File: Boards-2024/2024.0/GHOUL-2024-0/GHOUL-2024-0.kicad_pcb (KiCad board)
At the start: 4 copper layers, 91 parts, among them J1 USB_C_Receptacle_USB2.0, J2 U.FL, J3 SOICbite, J4 Conn_01x03_Pin, Q1 Q_NMOS_GSD, SW2 SLIDE, U1 MCU_RaspberryPi_RP2040_RP2040, U11 MAX-M10S, U2 TVS1800DRVR, U3 USBLC6-2SC6, U4 TPS2121RUXR, U5 W25Q128JVS, U6 LT6703CDC-3, U7 DRF1262TL, U8 MB85RS1MT, U9 MS5607-02BA, Y1 12MHz

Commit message: starting board layout
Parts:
- added TP1: TestPoint, TestPoint:TestPoint_Keystone_5000-5004_Miniature, F.Cu at (92.4, 73.8)
- added TP2: TestPoint, TestPoint:TestPoint_Keystone_5000-5004_Miniature, F.Cu at (92.5, 84.7)
- added U10: LTM4622AEV-PBF, GHOUL2024:LGA25_6P25X6P25_ADI, F.Cu at (89.5, 79.2)
- moved C23 132.4 mm to (160.1, 114.3), turned to -90 degrees
- moved C37 122.0 mm to (163.1, 144.0)
- moved AE1 122.0 mm to (178.7, 149.7)
- moved C35 122.0 mm to (163.0, 145.7)
- moved D2 122.0 mm to (159.4, 147.3)
- moved J4 122.0 mm to (160.2, 135.4)
- moved R24 122.0 mm to (178.3, 140.4)
- moved R28 122.0 mm to (159.7, 144.0)
- moved U11 122.0 mm to (170.7, 142.6)
- moved BT2 122.0 mm to (161.4, 140.0)
- moved R25 122.0 mm to (178.2, 138.8)
- moved U8 104.2 mm to (157.7, 117.8), turned to 90 degrees
- moved C16 79.8 mm to (113.8, 63.2)
- moved C17 78.1 mm to (112.0, 66.4)
- moved U2 77.8 mm to (113.6, 60.8)
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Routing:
- net +3V3: track 0.00 -> 23.2 mm, vias 0 -> 1
- net /QSPI_SS: track 0.00 -> 14.0 mm
- net GND: track 0.00 -> 13.0 mm, vias 0 -> 3
- net /QSPI_SD1: track 0.00 -> 12.8 mm
- net /QSPI_SD2: track 0.00 -> 11.4 mm
- net +1V1: track 0.00 -> 10.9 mm
- net Net-(U1-RUN): track 0.00 -> 9.54 mm
- net Net-(U1-XIN): track 0.00 -> 7.02 mm
- net Net-(U1-USB_DP): track 0.00 -> 6.58 mm
- net /QSPI_SD3: track 0.00 -> 6.24 mm
- net /RP_SWD: track 0.00 -> 6.07 mm
- net /RP_SWCLK: track 0.00 -> 5.69 mm
- net /FRAM_CS: track 0.00 -> 5.48 mm
- net /QSPI_SCLK: track 0.00 -> 4.91 mm
- net Net-(U1-USB_DM): track 0.00 -> 4.74 mm
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- added copper zone on In1.Cu, net GND
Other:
- board outline added: 60 x 60 mm

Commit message: finished connecting everything
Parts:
- added D3: LED, LED_SMD:LED_0603_1608Metric, F.Cu at (150.4, 138.3)
- added D4: LED, LED_SMD:LED_0603_1608Metric, F.Cu at (150.4, 145.2)
- added D5: LED, LED_SMD:LED_0603_1608Metric, F.Cu at (150.4, 141.8)
- added D6: LED, LED_SMD:LED_0603_1608Metric, F.Cu at (150.4, 134.8)
- added Q2: Q_NMOS_GSD, Package_TO_SOT_SMD:SOT-23-3, F.Cu at (146.7, 137.8)
- added Q3: Q_NMOS_GSD, Package_TO_SOT_SMD:SOT-23-3, F.Cu at (146.7, 144.7)
- added Q4: Q_NMOS_GSD, Package_TO_SOT_SMD:SOT-23-3, F.Cu at (146.7, 141.3)
- added Q5: Q_NMOS_GSD, Package_TO_SOT_SMD:SOT-23-3, F.Cu at (146.7, 134.3)
- added R27: 470, Resistor_SMD:R_0603_1608Metric, F.Cu at (150.4, 136.7)
- added R29: 470, Resistor_SMD:R_0603_1608Metric, F.Cu at (150.4, 143.7)
- added R30: 470, Resistor_SMD:R_0603_1608Metric, F.Cu at (150.4, 140.2)
- added R31: 470, Resistor_SMD:R_0603_1608Metric, F.Cu at (150.4, 133.2)
- C21, C22, J2, U7: moved to B.Cu
- moved H2 162.3 mm to (185.9, 154.0)
- moved H4 127.0 mm to (185.2, 84.3)
- moved R21 118.9 mm to (157.8, 107.1), turned to 90 degrees
- moved C27 118.8 mm to (165.3, 105.2), turned to 90 degrees
- moved H3 118.6 mm to (121.4, 159.0)
- moved R20 115.0 mm to (152.0, 108.7)
- moved C24 109.6 mm to (154.2, 106.7)
- moved L2 107.1 mm to (161.5, 106.4), turned to 180 degrees
- moved C21 101.0 mm to (156.5, 133.5)
- moved J2 101.0 mm to (160.7, 133.6)
- moved C22 97.7 mm to (156.6, 131.8)
- moved L1 97.1 mm to (149.8, 105.1), turned to 90 degrees
- moved J1 94.7 mm to (176.3, 109.7), turned to 90 degrees
- moved R3 89.7 mm to (170.6, 113.3), turned to 90 degrees
- moved BT1 82.3 mm to (166.8, 97.1), turned to -90 degrees
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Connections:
- C25 pad 1: +3.3V -> Net-(C25-Pad1)
- C26 pad 1: +5V -> Net-(C26-Pad1)
- L1 pad 2: Net-(L1-Pad2) -> Net-(C26-Pad1)
- L2 pad 2: Net-(L2-Pad2) -> Net-(C25-Pad1)
- Q1 pad 1: /LED -> /LED5
- R20 pad 2: Net-(L1-Pad2) -> Net-(C26-Pad1)
- R21 pad 2: Net-(L2-Pad2) -> Net-(C25-Pad1)
- U1 pad 2: /LED -> /LED1
- U1 pad 3: unconnected-(U1-GPIO1-Pad3) -> /LED2
- U1 pad 4: unconnected-(U1-GPIO2-Pad4) -> /LED3
- U1 pad 5: unconnected-(U1-GPIO3-Pad5) -> /LED4
- U1 pad 6: unconnected-(U1-GPIO4-Pad6) -> /LED5
- U10 pad A1: +5V -> Net-(C26-Pad1)
- U10 pad B1: +5V -> Net-(C26-Pad1)
- U10 pad D1: +3.3V -> Net-(C25-Pad1)
- U10 pad E1: +3.3V -> Net-(C25-Pad1)
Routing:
- net GND: track 13.0 -> 116.5 mm, vias 3 -> 109
- net +3V3: track 23.2 -> 86.8 mm, vias 1 -> 13
- net VBUS: track 0.00 -> 49.0 mm, vias 0 -> 6
- net +5V: track 0.00 -> 43.7 mm, vias 0 -> 4
- net VCC: track 0.00 -> 36.7 mm
- net /LED1: track 0.00 -> 33.6 mm
- net /SCL: track 0.00 -> 33.4 mm, vias 0 -> 2
- net /SDA: track 0.00 -> 31.0 mm
- net /LED2: track 0.00 -> 29.6 mm
- net /DRF_DIO1: track 0.00 -> 29.4 mm, vias 0 -> 1
- net /DRF_BUSY: track 0.00 -> 27.5 mm, vias 0 -> 1
- net /LED3: track 0.00 -> 24.9 mm
- net /RDIO_RST: track 1.20 -> 23.8 mm
- net /LVC_CUTOFF: track 0.00 -> 20.7 mm, vias 0 -> 2
- net /LED4: track 0.00 -> 20.6 mm
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- added copper zone on In2.Cu, net +3V3
- added copper zone on In2.Cu, net +5V
- added copper zone on F.Cu, net +BATT
- added copper zone on B.Cu, net GND
- added copper zone on F.Cu, net GND
- added copper zone on F.Cu, net VBUS
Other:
- board size 60 x 60 mm -> 57 x 60 mm

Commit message: finished board
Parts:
- added J10: Conn_01x04, Connector_PinHeader_2.54mm:PinHeader_1x04_P2.54mm_Vertical, F.Cu at (156.9, 147.1)
- added J5: Conn_01x04, Connector_Molex:Molex_SL_171971-0004_1x04_P2.54mm_Vertical, B.Cu at (138.1, 98.9)
- added J6: Conn_01x03, Connector_Molex:Molex_SL_171971-0003_1x03_P2.54mm_Vertical, F.Cu at (138.1, 106.9)
- added J7: Conn_01x02, Connector_Molex:Molex_SL_171971-0002_1x02_P2.54mm_Vertical, F.Cu at (138.1, 132.2)
- added J8: Conn_01x02, Connector_Molex:Molex_SL_171971-0002_1x02_P2.54mm_Vertical, F.Cu at (138.1, 141.1)
- added J9: Conn_01x04, Connector_Molex:Molex_SL_171971-0004_1x04_P2.54mm_Vertical, F.Cu at (138.1, 118.4)
- added Q6: Q_NMOS_GSD, Package_TO_SOT_SMD:SC-59, F.Cu at (160.6, 112.9)
- added Q7: Q_NMOS_GSD, Package_TO_SOT_SMD:SC-59, F.Cu at (164.7, 112.9)
- added R32: 4.7k, Resistor_SMD:R_0603_1608Metric, F.Cu at (142.3, 115.7)
- moved SW2 1.18 mm to (144.2, 93.2)
- moved C7 0.81 mm to (145.3, 120.1), turned to -135 degrees
- moved C3 0.69 mm to (150.6, 126.6), turned to 0 degrees
- moved C8 0.43 mm to (146.2, 115.1)
- moved R1 0.26 mm to (150.7, 123.6)
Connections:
- U1 pad 15: unconnected-(U1-GPIO12-Pad15) -> /LED4
- U1 pad 17: unconnected-(U1-GPIO14-Pad17) -> /HEATER1
- U1 pad 18: unconnected-(U1-GPIO15-Pad18) -> /HEATER2
- U1 pad 27: unconnected-(U1-GPIO16-Pad27) -> /GPIO16
- U1 pad 30: unconnected-(U1-GPIO19-Pad30) -> /GPIO19
- U1 pad 34: unconnected-(U1-GPIO22-Pad34) -> /PGOOD_CUT
- U1 pad 35: unconnected-(U1-GPIO23-Pad35) -> /DATA_CUT
- U1 pad 4: /LED3 -> /GPIO2
- U1 pad 40: unconnected-(U1-GPIO28_ADC2-Pad40) -> /CUT_CURR
- U1 pad 5: /LED4 -> /GPIO3
- U1 pad 7: unconnected-(U1-GPIO5-Pad7) -> /SERVO_PWM
- U1 pad 8: unconnected-(U1-GPIO6-Pad8) -> /TEMP
- U1 pad 9: unconnected-(U1-GPIO7-Pad9) -> /LED3
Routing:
- net /GPIO3: track 0.00 -> 51.9 mm, vias 0 -> 2
- net /GPIO2: track 0.00 -> 50.8 mm, vias 0 -> 2
- net Net-(J8-Pin_2): track 0.00 -> 50.5 mm, vias 0 -> 1
- net Net-(J7-Pin_2): track 0.00 -> 45.1 mm, vias 0 -> 1
- net +5V: track 43.7 -> 87.0 mm
- net /SERVO_PWM: track 0.00 -> 40.8 mm, vias 0 -> 1
- net /GPIO19: track 0.00 -> 33.9 mm, vias 0 -> 2
- net GND: track 116.5 -> 149.2 mm, vias 109 -> 119
- net /GPIO16: track 0.00 -> 28.8 mm, vias 0 -> 1
- net /TEMP: track 0.00 -> 28.0 mm, vias 0 -> 2
- net /HEATER2: track 0.00 -> 26.3 mm, vias 0 -> 2
- net /DATA_CUT: track 0.00 -> 23.7 mm, vias 0 -> 2
- net /CUT_CURR: track 0.00 -> 22.6 mm, vias 0 -> 1
- net /PGOOD_CUT: track 0.00 -> 21.7 mm, vias 0 -> 1
- net +3V3: track 86.8 -> 106.5 mm, vias 13 -> 20
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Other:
- board outline removed

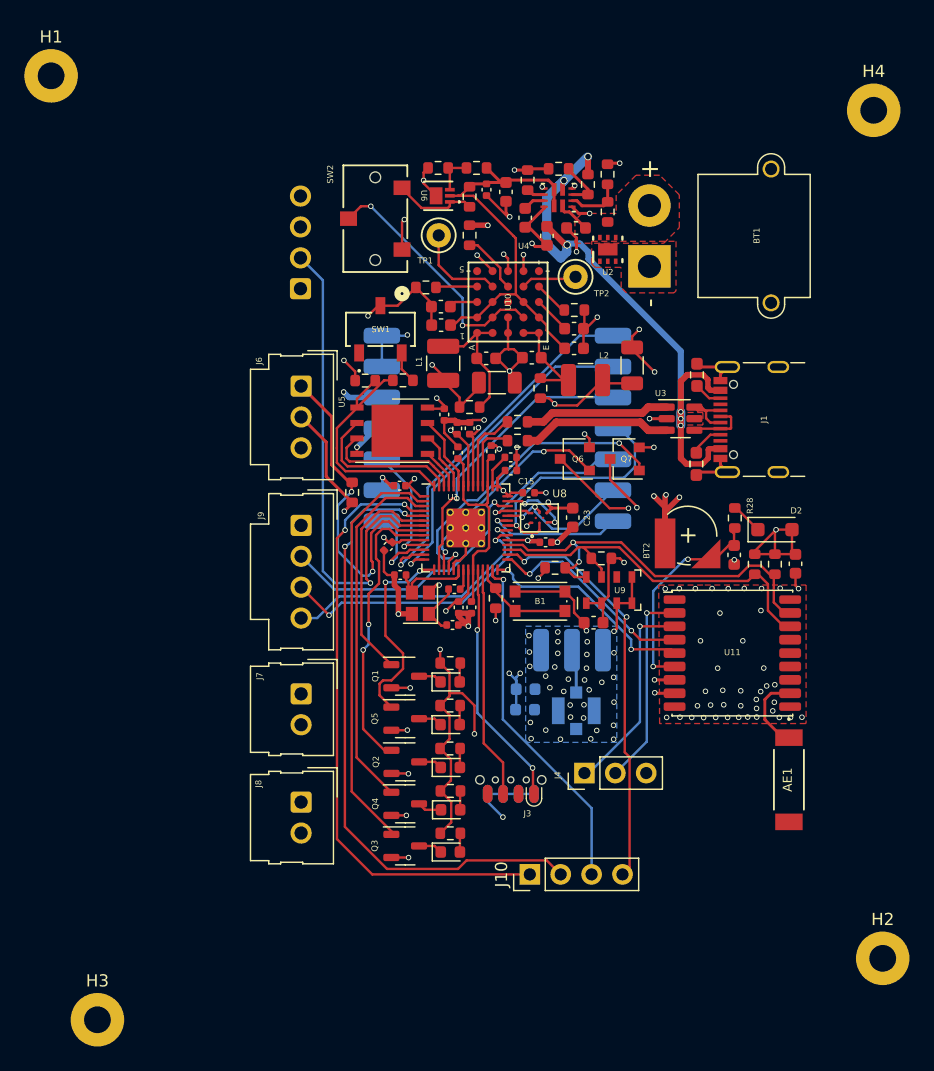
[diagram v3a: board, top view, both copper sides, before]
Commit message: Finished board outline
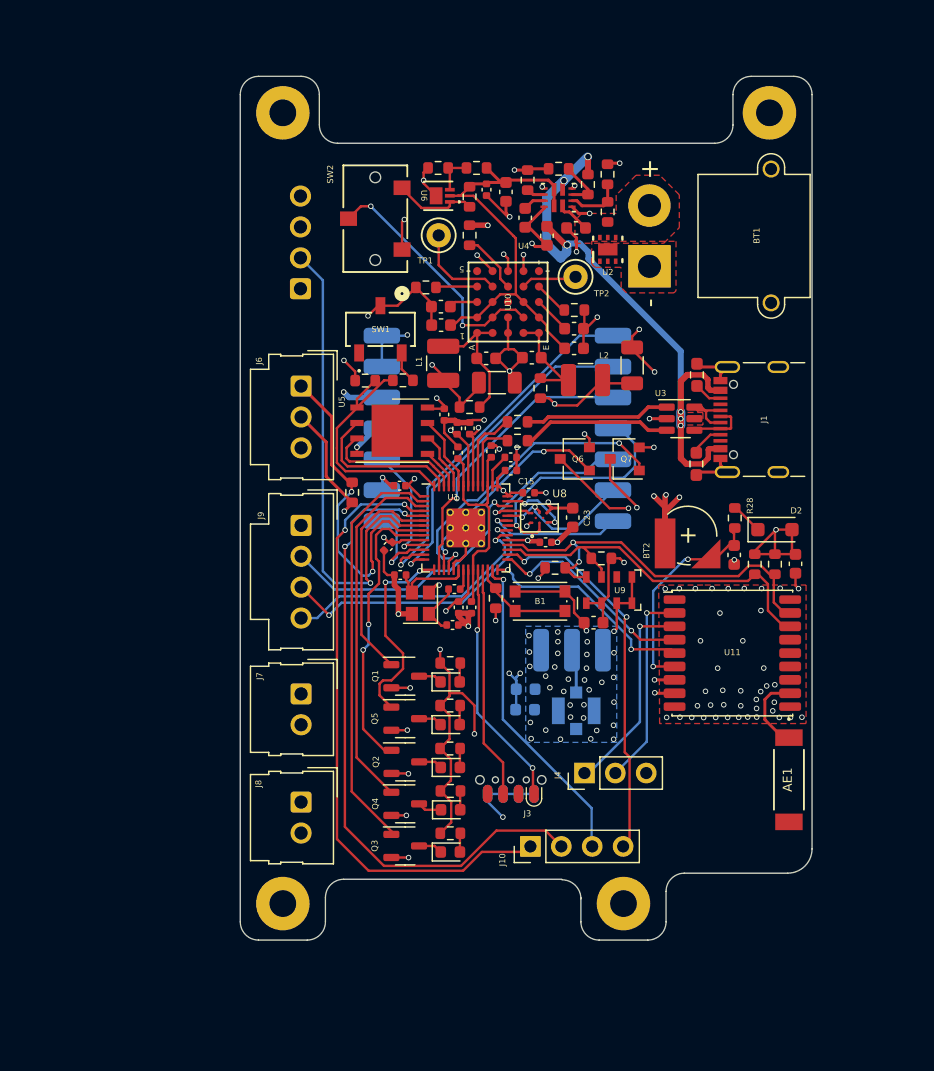
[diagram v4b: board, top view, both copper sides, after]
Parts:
- moved H2 49.5 mm to (136.6, 149.5)
- moved H3 44.3 mm to (164.6, 149.5)
- moved H1 19.3 mm to (136.6, 84.5)
- moved H4 8.57 mm to (176.6, 84.5)
- moved J10 2.30 mm to (157.0, 144.8)
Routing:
- net /GPIO19: track 33.9 -> 31.5 mm
- net /GPIO16: track 28.8 -> 26.5 mm
- net /GPIO3: track 51.9 -> 53.2 mm
- net /GPIO2: track 50.8 -> 51.5 mm
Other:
- board outline added: 47 x 71 mm

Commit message: ready for shipman review
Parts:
- C25, C26: footprint Capacitor_SMD:C_0603_1608Metric -> Capacitor_SMD:C_0805_2012Metric
- moved C21 31.8 mm to (140.7, 106.0), turned to 180 degrees
- moved C22 31.7 mm to (140.7, 104.4), turned to 180 degrees
- moved R21 0.37 mm to (157.8, 107.5)
- moved C24 0.23 mm to (154.1, 106.8)
- moved C25 0.17 mm to (157.3, 104.6)
- moved J6 0.15 mm to (138.0, 106.8)
- moved R20 0.13 mm to (152.0, 108.8)
- moved C26 0.11 mm to (153.3, 104.5)
- moved C14 0.11 mm to (152.0, 110.5)
- moved C11 0.11 mm to (151.0, 110.5)
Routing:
- net GND: track 149.2 -> 161.1 mm, vias 119 -> 126
- net +5V: track 87.0 -> 82.6 mm, vias 4 -> 5
- net +3V3: track 106.5 -> 105.5 mm, vias 20 -> 21
- net /LVC_CUTOFF: track 21.0 -> 21.7 mm
- added copper zone on F.Cu, net +3V3
- added copper zone on F.Cu, net +5V
- added copper zone on In2.Cu, net GND
- added copper zone on F.Cu, net Net-(C25-Pad1)
- added copper zone on F.Cu, net VCC
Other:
- outline, holes or cut-outs redrawn

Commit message: almost as good as garlic honey chicken
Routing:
- net VBUS: track 52.8 -> 49.3 mm
- net GND: track 161.1 -> 162.0 mm
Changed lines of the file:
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@@
   (segment (start 155.675 89.175) (end 155.67 89.17) (width 0.25) (layer "F.Cu") (net 2))
   (segment (start 146.428101 95.71) (end 146.428101 93.431899) (width 1) (layer "F.Cu") (net 2))
+  (segment (start 160.7 94.679998) (end 159.955001 93.934999) (width 0.25) (layer "F.Cu") (net 2))
   (segment (start 150.67 122.0275) (end 150.67 121.495025) (width 0.2) (layer "F.Cu") (net 2))
   (segment (start 164.075 126.825) (end 164.075 124.775) (width 0.2) (layer "F.Cu") (net 2))
@@
   (segment (start 151.06 126.57) (end 151.78 126.57) (width 0.2) (layer "F.Cu") (net 2))
   (segment (start 165.34 103.755) (end 165.34 103.92) (width 0.2) (layer "F.Cu") (net 2))
-  (segment (start 160.77 94.749998) (end 160.77 95.89) (width 0.25) (layer "F.Cu") (net 2))
   (segment (start 156.855 89.07) (end 156.75 89.175) (width 0.25) (layer "F.Cu") (net 2))
   (segment (start 161.345 102.21) (end 161.54 102.21) (width 0.2) (layer "F.Cu") (net 2))
@@
   (segment (start 158.34 95.355) (end 158.235 95.46) (width 0.25) (layer "F.Cu") (net 2))
   (segment (start 178.77 123.33) (end 179.02 123.58) (width 0.2) (layer "F.Cu") (net 2))
-  (segment (start 159.955001 93.934999) (end 160.77 94.749998) (width 0.25) (layer "F.Cu") (net 2))
+  (segment (start 160.22995 96.09) (end 160.7 95.61995) (width 0.25) (layer "F.Cu") (net 2))
   (segment (start 172.6 113.425) (end 173.175 114) (width 0.25) (layer "F.Cu") (net 2))
   (segment (start 154.12 104.655) (end 154.225 104.655) (width 0.2) (layer "F.Cu") (net 2))
@@
   (segment (start 158.71 119.77) (end 159.205 119.77) (width 0.45) (layer "F.Cu") (net 2))
   (segment (start 165.325 122.625) (end 165.325 124.775) (width 0.2) (layer "F.Cu") (net 2))
+  (segment (start 160.7 95.61995) (end 160.7 94.679998) (width 0.25) (layer "F.Cu") (net 2))
   (segment (start 148.845 101.9) (end 148.865 101.92) (width 0.2) (layer "F.Cu") (net 2))
   (segment (start 155.265 105.695) (end 155.265 106.55) (width 0.2) (layer "F.Cu") (net 2))
   (segment (start 154.225 104.655) (end 155.265 105.695) (width 0.2) (layer "F.Cu") (net 2))
   (segment (start 158.235 95.46) (end 157.78 95.46) (width 0.25) (layer "F.Cu") (net 2))
+  (segment (start 159.63 96.09) (end 160.22995 96.09) (width 0.25) (layer "F.Cu") (net 2))
   (segment (start 144.951178 120.448822) (end 144.9395 120.4605) (width 0.2) (layer "F.Cu") (net 2))
   (segment (start 150.875025 121.29) (end 151.16 121.29) (width 0.2) (layer "F.Cu") (net 2))
@@
   (via (at 176.4 131.58) (size 0.45) (drill 0.3) (layers "F.Cu" "B.Cu") (free) (net 2))
   (via (at 158.98 130.02) (size 0.45) (drill 0.3) (layers "F.Cu" "B.Cu") (free) (net 2))
-  (via (at 160.77 95.89) (size 0.45) (drill 0.3) (layers "F.Cu" "B.Cu") (net 2))
+  (via (at 159.63 96.09) (size 0.45) (drill 0.3) (layers "F.Cu" "B.Cu") (net 2))
   (via (at 146.428101 93.431899) (size 0.75) (drill 0.6) (layers "F.Cu" "B.Cu") (net 2))
   (via (at 165.93 102.27) (size 0.45) (drill 0.3) (layers "F.Cu" "B.Cu") (net 2))
@@
   (via (at 160 95.33) (size 0.75) (drill 0.6) (layers "F.Cu" "B.Cu") (net 10))
   (segment (start 161.752703 96.622703) (end 161.752703 95.592703) (width 0.75) (layer "B.Cu") (net 10))
-  (segment (start 161.25 95.09) (end 160.24 95.09) (width 0.75) (layer "B.Cu") (net 10))
+  (segment (start 159.3 90.36) (end 161.56 88.1) (width 1) (layer "B.Cu") (net 10))
   (segment (start 161.71 88.07) (end 161.66 88.12) (width 0.5) (layer "B.Cu") (net 10))
-  (segment (start 158.32 91.46) (end 158.32 95.26) (width 0.75) (layer "B.Cu") (net 10))
+  (segment (start 161.56 88.1) (end 161.68 88.1) (width 1) (layer "B.Cu") (net 10))
+  (segment (start 160.68 93.85) (end 159.3 92.47) (width 1) (layer "B.Cu") (net 10))
   (segment (start 160.115 95.215) (end 160 95.33) (width 0.5) (layer "B.Cu") (net 10))
-  (segment (start 159.97 95.36) (end 160 95.33) (width 0.75) (layer "B.Cu") (net 10))
   (segment (start 161.68 88.09) (end 161.69 88.09) (width 0.5) (layer "B.Cu") (net 10))
   (segment (start 161.752703 95.592703) (end 161.25 95.09) (width 0.75) (layer "B.Cu") (net 10))
   (segment (start 161.68 88.1) (end 161.68 88.09) (width 0.5) (layer "B.Cu") (net 10))
   (segment (start 169.34 109.05) (end 169.34 110.17) (width 0.75) (layer "B.Cu") (net 10))
-  (segment (start 159.465 96.405) (end 159.97 95.9) (width 0.75) (layer "B.Cu") (net 10))
-  (segment (start 158.32 95.26) (end 159.465 96.405) (width 0.75) (layer "B.Cu") (net 10))
   (segment (start 169.34 110.17) (end 169.34 104.21) (width 0.75) (layer "B.Cu") (net 10))
+  (segment (start 161.25 95.09) (end 160.68 95.09) (width 0.75) (layer "B.Cu") (net 10))
+  (segment (start 160.68 95.09) (end 160.24 95.09) (width 0.75) (layer "B.Cu") (net 10))
   (segment (start 161.69 88.09) (end 161.71 88.07) (width 0.5) (layer "B.Cu") (net 10))
-  (segment (start 159.7355 90.0445) (end 159.3 90.48) (width 0.75) (layer "B.Cu") (net 10))
+  (segment (start 160.68 95.09) (end 160.68 93.85) (width 1) (layer "B.Cu") (net 10))
+  (segment (start 159.3 92.47) (end 159.3 90.36) (width 1) (layer "B.Cu") (net 10))
   (segment (start 160.24 95.09) (end 160.115 95.215) (width 0.75) (layer "B.Cu") (net 10))
-  (segment (start 159.3 90.48) (end 158.32 91.46) (width 0.75) (layer "B.Cu") (net 10))
-  (segment (start 159.97 95.9) (end 159.97 95.36) (width 0.75) (layer "B.Cu") (net 10))
   (segment (start 169.34 104.21) (end 161.752703 96.622703) (width 0.75) (layer "B.Cu") (net 10))
-  (segment (start 159.3 90.48) (end 161.68 88.1) (width 0.75) (layer "B.Cu") (net 10))
   (segment (start 158.100002 91.69) (end 157.185 91.69) (width 0.25) (layer "F.Cu") (net 11))
   (segment (start 157.185 91.69) (end 156.55 92.325) (width 0.25) (layer "F.Cu") (net 11))
